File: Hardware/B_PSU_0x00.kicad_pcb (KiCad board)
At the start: 2 copper layers, 101.1 x 52.5 mm, 82 parts, among them J1 Conn_01x03, J10 Conn_01x02, J11 Conn_01x03, J12 Conn_01x03, J13 Conn_01x03, J14 Conn_01x02, J15 Conn_01x02, J16 Conn_01x02, J17 Conn_01x02, J18 Conn_01x03, J19 Conn_01x03, J2 Conn_01x02, J20 Conn_01x03, J21 Conn_01x03, J22 Conn_01x03, J23 Conn_01x02, J24 Conn_01x02, J25 Conn_01x02, J26 Conn_01x02, J27 Conn_01x03, J28 Conn_01x03, J3 Conn_01x03, J4 Conn_01x03, J5 Conn_01x03, J6 Conn_01x03, J7 Conn_01x02, J8 Conn_01x02, J9 Conn_01x02, U1 ADP5070AREZ, U2 ADP7118WAUJZ-5.0, U3 ADP7118AUJZ-3.3-R7, U4 ADP7142AUJZ-1.8, U5 ADP7118AUJZ-2.5-R7, U6 ADP7182ACPZ-5.0-R7, U7 ADP7183ACPZN3.3-R7, U8 ADP7182ACPZN-2.5R7, U9 ADP7182AUJZ-1.8

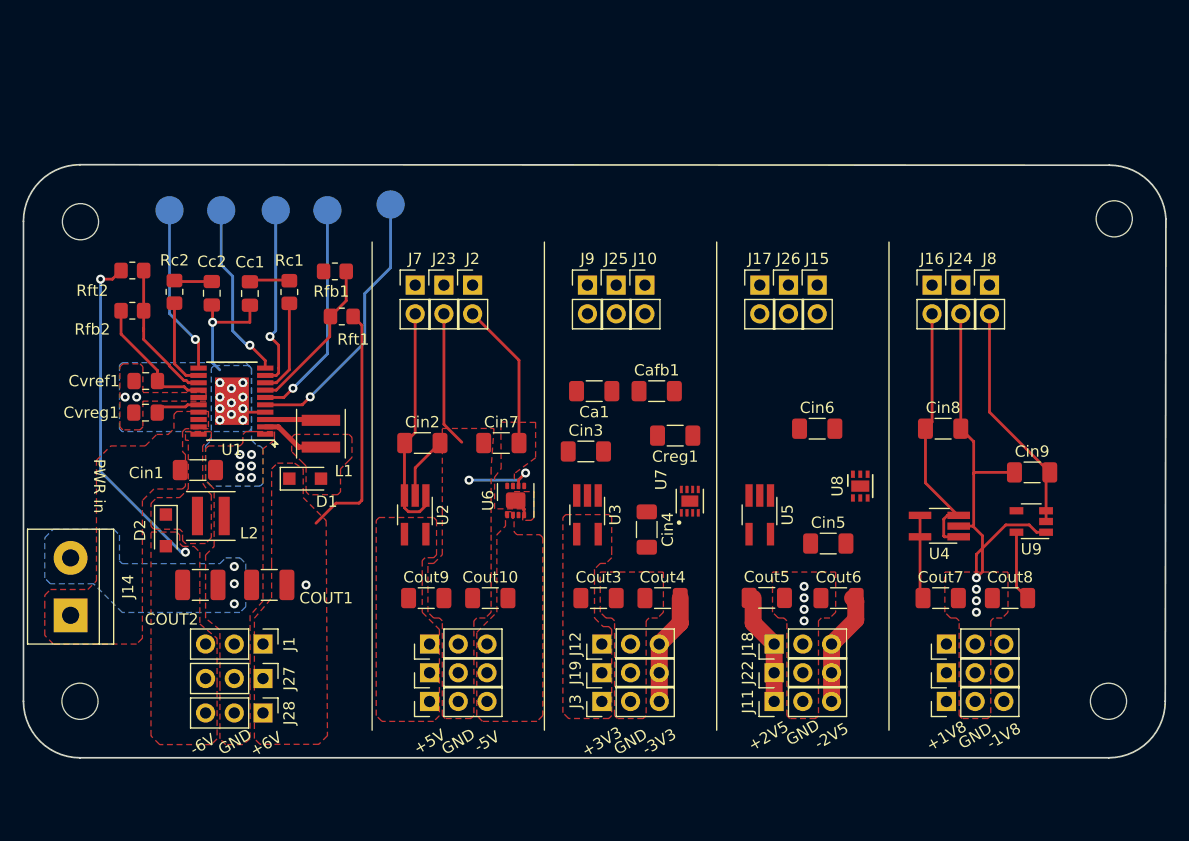
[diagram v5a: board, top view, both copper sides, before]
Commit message: changed the layout and the size of the PCB
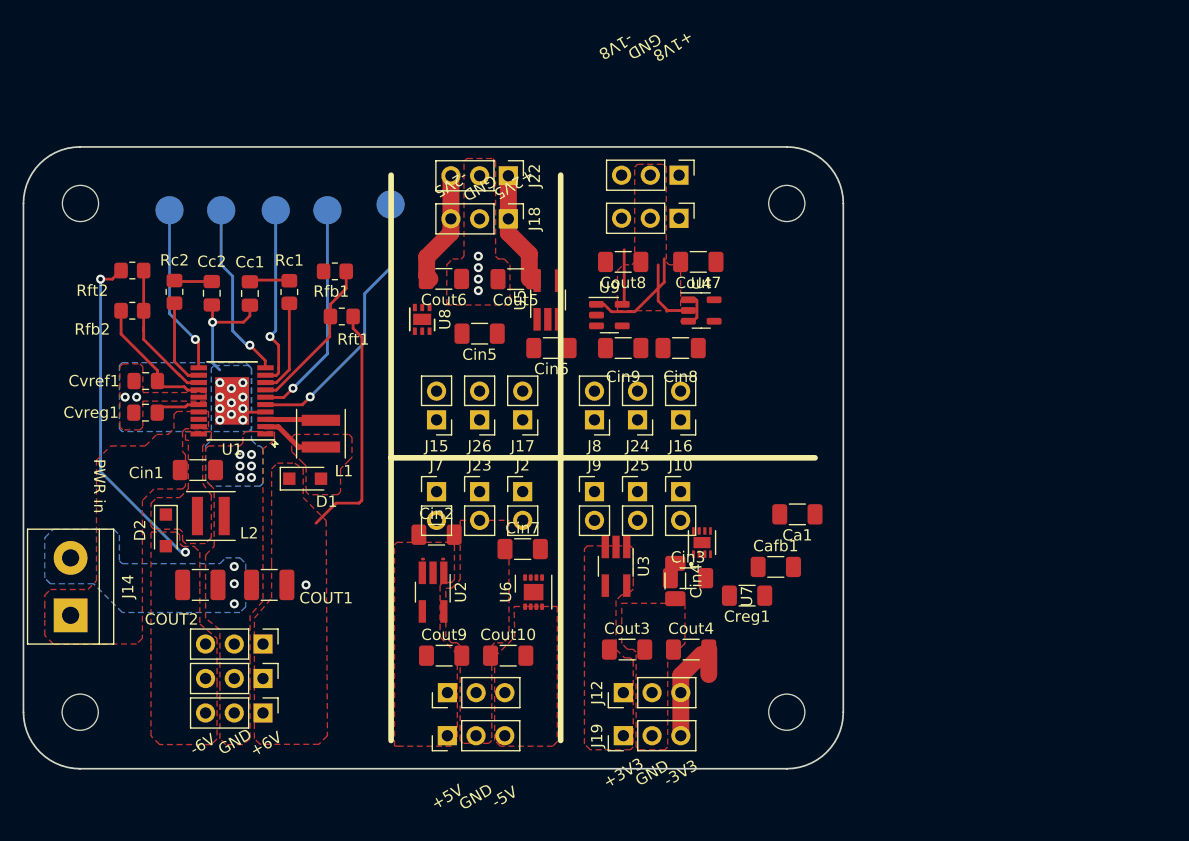
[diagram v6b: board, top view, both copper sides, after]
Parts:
- removed J11, J3, J4, J5: Conn_01x03, Connector_PinHeader_2.54mm:PinHeader_1x03_P2.54mm_Vertical
- U4: footprint Package_TO_SOT_SMD:TSOT-23-5_HandSoldering -> Package_TO_SOT_SMD:TSOT-23-5
- moved J13 50.0 mm to (118.0, 82.5), turned to -90 degrees
- moved J22 49.9 mm to (102.9, 82.5), turned to -90 degrees
- moved Cout8 45.3 mm to (113.0, 90.2), turned to 180 degrees
- moved Cout6 44.9 mm to (97.2, 91.7), turned to 180 degrees
- moved J21 44.5 mm to (118.0, 86.3), turned to -90 degrees
- moved J18 44.4 mm to (102.9, 86.4), turned to -90 degrees
- moved U9 41.5 mm to (111.8, 94.9), turned to 0 degrees
- moved U8 41.5 mm to (95.2, 95.2), turned to -90 degrees
- moved Cin9 37.8 mm to (113.0, 97.8), turned to 180 degrees
- moved J8 36.9 mm to (110.5, 104.1), turned to 180 degrees
- moved Cout7 36.7 mm to (119.7, 90.2), turned to 180 degrees
- moved Cin5 36.0 mm to (100.3, 96.5), turned to 180 degrees
- moved Cout5 35.9 mm to (103.5, 91.7), turned to 180 degrees
- moved J15 35.7 mm to (96.5, 104.1), turned to 180 degrees
- moved J24 31.0 mm to (114.3, 104.1), turned to 180 degrees
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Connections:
- Ca1 pad 2: Net-(Cin3-Pad2) -> /GND_3v3
- Cin2 pad 1: /EN_+5v -> /Vin_+5v
- Cin2 pad 2: Net-(Cin2-Pad2) -> /GND_5v
- Cin3 pad 2: Net-(Cin3-Pad2) -> /GND_3v3
- Cin4 pad 2: Net-(Cin3-Pad2) -> /GND_3v3
- Cin5 pad 2: Net-(Cin5-Pad2) -> /GND_2v5
- Cin6 pad 2: Net-(Cin5-Pad2) -> /GND_2v5
- Cin7 pad 1: Net-(Cin2-Pad2) -> /GND_5v
- Cin7 pad 2: /EN_-5v -> /Vin_-5v
- Cin8 pad 2: Net-(Cin8-Pad2) -> /GND_1v8
- Cin9 pad 1: Net-(Cin8-Pad2) -> /GND_1v8
- Cout10 pad 1: Net-(Cin2-Pad2) -> /GND_5v
- Cout3 pad 2: Net-(Cin3-Pad2) -> /GND_3v3
- Cout4 pad 1: Net-(Cin3-Pad2) -> /GND_3v3
- Cout5 pad 2: Net-(Cin5-Pad2) -> /GND_2v5
- Cout6 pad 1: Net-(Cin5-Pad2) -> /GND_2v5
- Cout7 pad 2: Net-(Cin8-Pad2) -> /GND_1v8
- Cout8 pad 1: Net-(Cin8-Pad2) -> /GND_1v8
- Cout9 pad 2: Net-(Cin2-Pad2) -> /GND_5v
- Creg1 pad 2: Net-(Cin3-Pad2) -> /GND_3v3
- J10 pad 1: /Vin_-3v3 -> /EN_-3v3
- J12 pad 2: Net-(Cin3-Pad2) -> /GND_3v3
- J13 pad 2: Net-(Cin8-Pad2) -> /GND_1v8
- J15 pad 1: /Vin_-2v5 -> /EN_-2v5
- J16 pad 1: /Vin_+1v8 -> /EN_+1v8
- J17 pad 1: /Vin_+2v5 -> /EN_+2v5
- J18 pad 2: Net-(Cin5-Pad2) -> /GND_2v5
- J19 pad 2: Net-(Cin3-Pad2) -> /GND_3v3
- J2 pad 2: /EN_-5v -> /Vin_-5v
- J20 pad 2: Net-(Cin2-Pad2) -> /GND_5v
- J21 pad 2: Net-(Cin8-Pad2) -> /GND_1v8
- J22 pad 2: Net-(Cin5-Pad2) -> /GND_2v5
- J23 pad 2: Net-(Cin2-Pad2) -> /GND_5v
- J24 pad 2: Net-(Cin8-Pad2) -> /GND_1v8
- J25 pad 2: Net-(Cin3-Pad2) -> /GND_3v3
- J26 pad 2: Net-(Cin5-Pad2) -> /GND_2v5
- J6 pad 2: Net-(Cin2-Pad2) -> /GND_5v
- J7 pad 2: /EN_+5v -> /Vin_+5v
- J8 pad 1: /Vin_-1v8 -> /EN_-1v8
- J9 pad 1: /Vin_+3v3 -> /EN_+3v3
- U2 pad 1: /EN_+5v -> /Vin_+5v
- U2 pad 2: Net-(Cin2-Pad2) -> /GND_5v
- U2 pad 3: /EN_+5v -> /Vin_+5v
- U3 pad 2: Net-(Cin3-Pad2) -> /GND_3v3
- U4 pad 2: Net-(Cin8-Pad2) -> /GND_1v8
- U5 pad 2: Net-(Cin5-Pad2) -> /GND_2v5
- U6 pad 4: /EN_-5v -> /Vin_-5v
- U6 pad 6: Net-(Cin2-Pad2) -> /GND_5v
- U6 pad 7: /EN_-5v -> /Vin_-5v
- U6 pad 8: /EN_-5v -> /Vin_-5v
- U6 pad 9: /EN_-5v -> /Vin_-5v
- U8 pad 5: Net-(Cin5-Pad2) -> /GND_2v5
- U9 pad 1: Net-(Cin8-Pad2) -> /GND_1v8
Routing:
- net Net-(Cin8-Pad2): track 38.9 -> 0.00 mm, vias 4 -> 0
- net Net-(Cin2-Pad2): track 24.2 -> 0.00 mm, vias 2 -> 0
- net /EN_+1v8: track 23.6 -> 0.00 mm
- net /EN_-1v8: track 20.7 -> 0.00 mm
- net /EN_+5v: track 20.7 -> 0.00 mm
- net /GND_1v8: track 0.00 -> 19.7 mm
- net /EN_-5v: track 14.7 -> 0.00 mm
- net /+1v8: track 7.43 -> 0.00 mm
- net /-1v8: track 6.24 -> 4.83 mm
- net /+5V: track 0.64 -> 0.00 mm
- net Net-(Cin5-Pad2): vias 4 -> 0
- net /GND_2v5: vias 0 -> 4
- added copper zone on F.Cu, net /GND_1v8
- added copper zone on F.Cu, net /GND_2v5
- added copper zone on F.Cu, net /GND_3v3
- added copper zone on F.Cu, net /GND_5v
- removed copper zone on F.Cu, net /EN_-5v
- removed copper zone on F.Cu, net Net-(Cin2-Pad2)
- removed copper zone on F.Cu, net Net-(Cin3-Pad2)
- removed copper zone on F.Cu, net Net-(Cin5-Pad2)
- removed copper zone on F.Cu, net Net-(Cin8-Pad2)
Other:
- board size 101.1 x 52.5 mm -> 72.5 x 55 mm

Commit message: small updates
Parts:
- moved Cin3 44.7 mm to (111.0, 74.2)
- moved Cin4 44.2 mm to (116.3, 74.2), turned to 180 degrees
- moved Cout5 43.2 mm to (102.9, 48.5)
- moved Cout6 43.2 mm to (96.4, 48.5)
- moved Cin6 42.8 mm to (96.8, 56.1), turned to 0 degrees
- moved U8 42.2 mm to (95.2, 53.1), turned to 0 degrees
- moved COUT1 41.9 mm to (81.0, 76.8)
- moved COUT2 41.9 mm to (74.9, 76.8)
- moved Creg1 41.9 mm to (123.2, 77.8)
- moved J12 41.9 mm to (112.3, 86.4)
- moved J19 41.9 mm to (112.3, 90.2)
- moved J20 41.9 mm to (96.7, 90.2)
- moved J28 41.9 mm to (80.4, 88.2)
- moved J6 41.9 mm to (96.7, 86.4)
- moved Cin8 41.9 mm to (117.3, 55.9)
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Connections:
- net /Vin_+5v renamed /EN_+5v
- net /Vin_-5v renamed /EN_-5v
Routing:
- net /GND_1v8: track 19.7 -> 0.00 mm
- net /-2v5: track 10.2 -> 0.00 mm
- net /-3v3: track 9.91 -> 0.00 mm
- net /+2v5: track 9.91 -> 0.00 mm
- net GNDA: track 12.6 -> 6.63 mm, vias 23 -> 25
- net /EN_-5v: track 0.00 -> 5.91 mm
- net /-1v8: track 4.83 -> 0.00 mm
- net /GND_3v3: track 0.00 -> 3.85 mm
- net /GND_5v: track 0.00 -> 3.26 mm
- net /Vpoz: vias 1 -> 0
- net /GND_2v5: vias 4 -> 0
- added copper zone on F.Cu, net /EN_+3v3
- added copper zone on F.Cu, net /EN_+5v
- added copper zone on F.Cu, net /EN_-2v5
- added copper zone on F.Cu, net /EN_-5v

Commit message: small updates
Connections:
- net /-2v5 renamed Net-(J18-Pin_3)
- Cout4 pad 2: /-3v3 -> Net-(J12-Pin_3)
- J12 pad 3: /-3v3 -> Net-(J12-Pin_3)
- J19 pad 3: /-3v3 -> Net-(J12-Pin_3)
